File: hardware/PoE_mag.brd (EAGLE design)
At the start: 149.9 x 124.5 mm, 126 parts, among them IC1 LD1117V33, IC10 74LVC1T45SOT23-HAND, IC11 74LVC1T45SOT23-HAND, IC12 PCA9517A, IC2 LD1117V33, IC3 DS1338, IC4 ATMEGA1284, IC5 TSR 1-2450, IC6 LM61, IC7 MCP2200, IC8 74LVC1T45SOT23-HAND, IC9 74LVC1T45SOT23-HAND, Q1 BSS138, Q2 BUK98150-55A, X1 PWR, X2 JTAG, X3 USB, X4 MICRO-SD-SOCKETHIROSE-DM3D, X5 CONN-SMATHD, X6 UFL, X7 22-23-2021, X8 RJ45, X9 RJ11, Y1 32k768, Y2 16MHz, Y3 12MHz

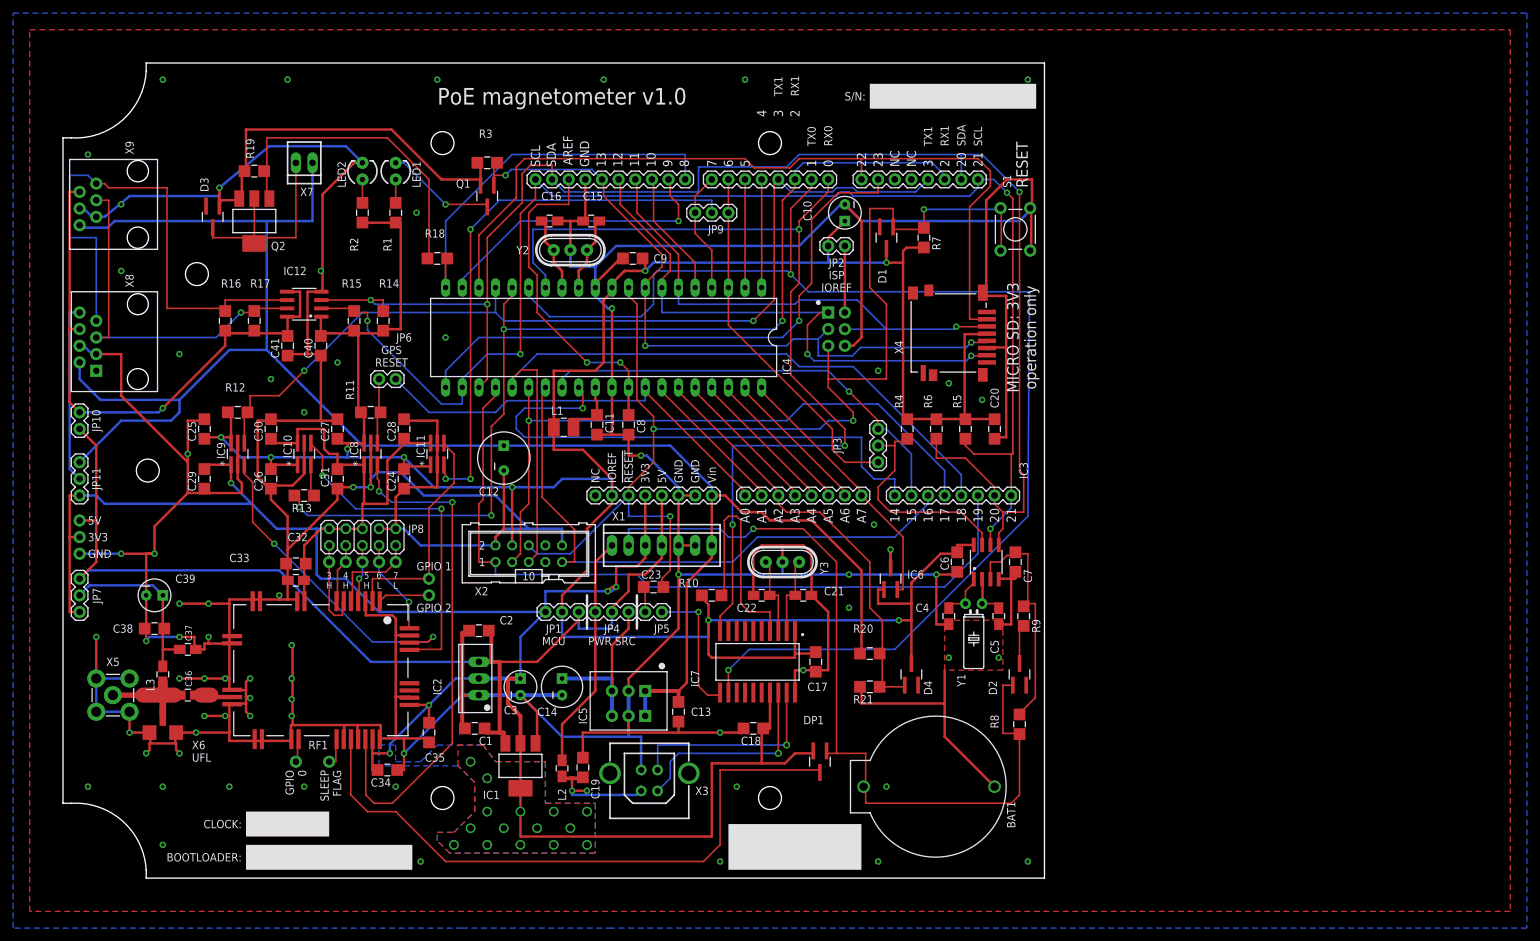
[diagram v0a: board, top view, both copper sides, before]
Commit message: Move battery holder
Move to create more room so that alternative versions can be used.
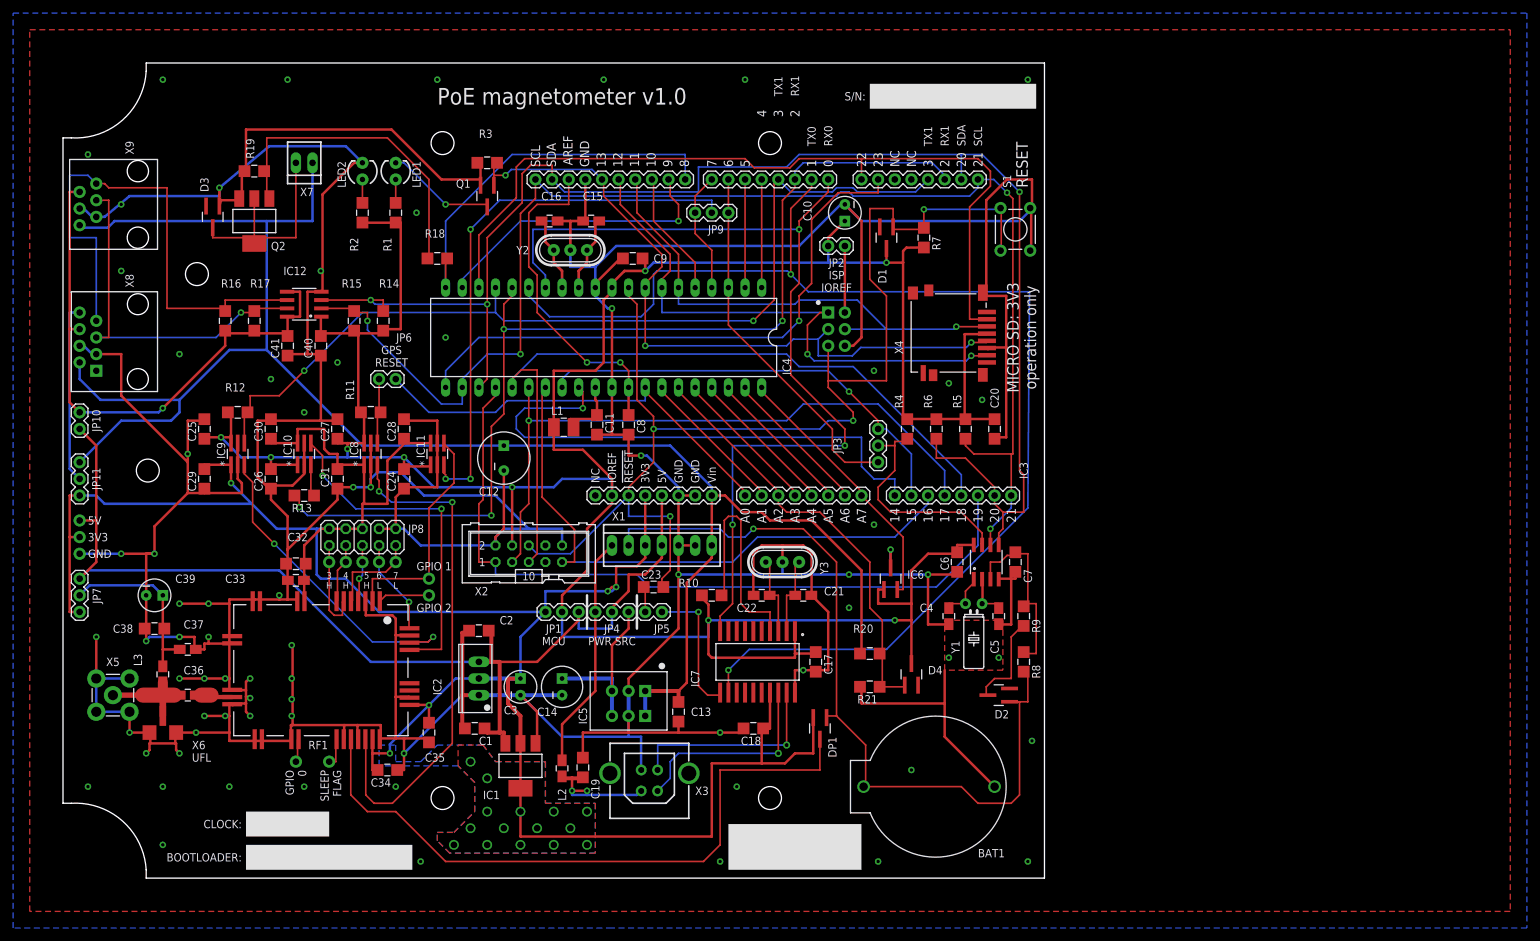
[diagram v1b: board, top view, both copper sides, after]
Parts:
- BAT1: device SparkFun:BATTCOM_20MM_PTH -> SteveMarple:BATTCOM_20MM_PTH
- moved R8 9.55 mm to (146.7, 20.3)
- moved DP1 5.08 mm to (115.6, 10.2)
- moved D2 4.49 mm to (142.9, 15.2), turned to 180 degrees
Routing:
- net N$9: track 6.00 -> 15.1 mm
- net N$11: track 38.3 -> 30.8 mm
- net +3V3: track 370.9 -> 376.0 mm
- net V_BACKUP: track 97.3 -> 101.5 mm
- net VBATT: track 125.8 -> 123.0 mm
- net GND: track 1208.1 -> 1209.3 mm, vias 73 -> 74
- net VCC: track 471.6 -> 472.8 mm
- net 19(TCK): track 117.6 -> 116.9 mm
- net 1(TX0): track 194.9 -> 194.1 mm

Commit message: Update crystal value
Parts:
- Y2: value 16MHz -> 12MHz
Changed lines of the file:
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@@
 <attribute name="VALUE" x="74.93" y="20.955" size="1.27" layer="27" ratio="10" align="bottom-center"/>
 </element>
-<element name="Y2" library="SteveMarple" package="HC49U-V-RESONATOR" value="16MHz" x="77.47" y="83.185" smashed="yes" rot="R180">
+<element name="Y2" library="SteveMarple" package="HC49U-V-RESONATOR" value="12MHz" x="77.47" y="83.185" smashed="yes" rot="R180">
 <attribute name="NAME" x="69.215" y="82.55" size="1.27" layer="25" ratio="10"/>
 <attribute name="VALUE" x="66.04" y="83.185" size="1.27" layer="27" ratio="10" display="off"/>

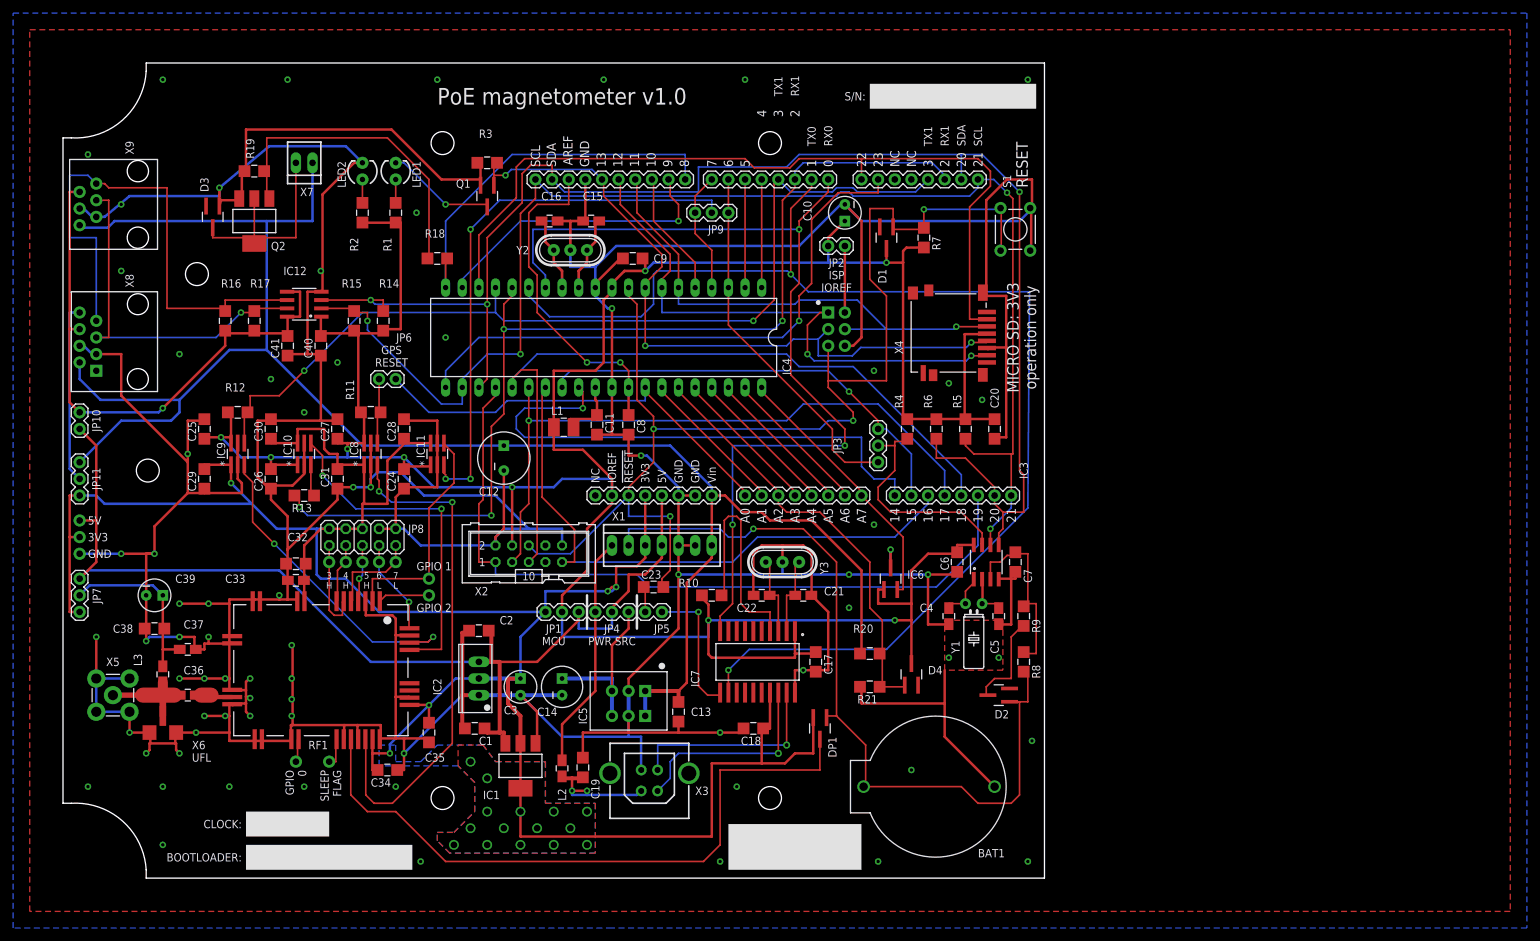
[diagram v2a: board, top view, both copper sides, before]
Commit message: Increase dia of mounting holes, increase thermal reliefs
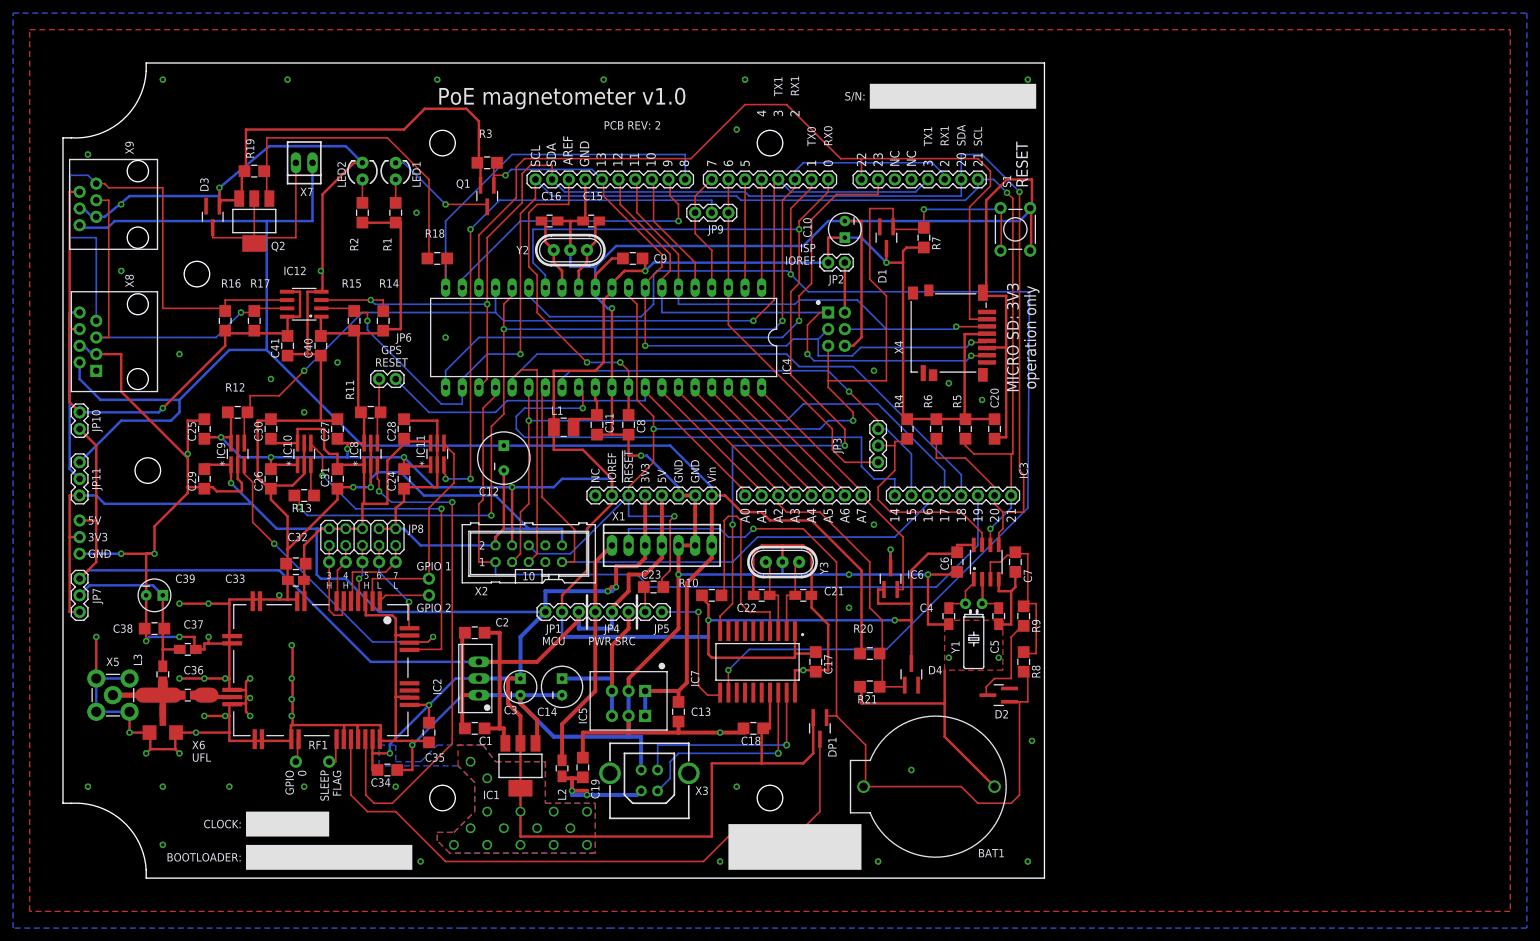
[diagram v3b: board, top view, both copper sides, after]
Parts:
- moved C10 2.54 mm to (119.4, 86.4)
- moved JP2 2.54 mm to (119.4, 81.3)
- moved C2 0.71 mm to (62.9, 24.8)
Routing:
- net 22: track 125.4 -> 131.1 mm
- net V_BACKUP: track 101.5 -> 98.6 mm
- net VCC: track 472.8 -> 470.1 mm
- net N$6: track 10.2 -> 7.62 mm
- net 20(SDA): track 231.8 -> 230.0 mm
- net +5V: track 167.7 -> 168.9 mm
- net !RESET: track 189.6 -> 190.5 mm
- net GND: track 1209.3 -> 1210.2 mm, vias 74 -> 75
- net 3(TX1): track 142.5 -> 142.0 mm
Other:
- board text added: "PCB REV: 2"
